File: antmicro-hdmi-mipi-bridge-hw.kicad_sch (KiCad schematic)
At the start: 0 parts

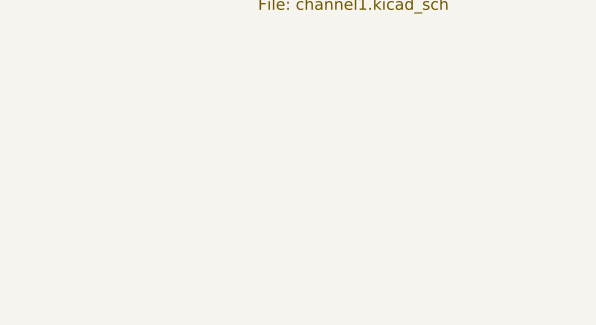
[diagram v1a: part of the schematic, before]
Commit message: [#58304] Fix DRC
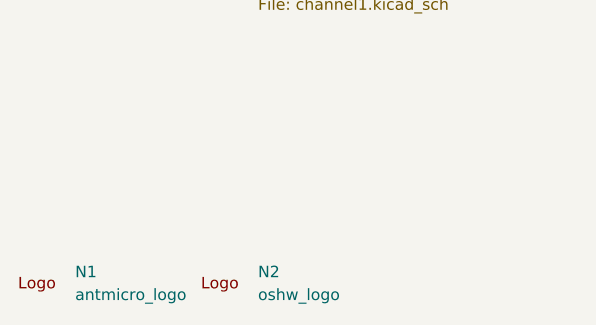
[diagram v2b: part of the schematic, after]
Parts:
- added N1: antmicro_logo, antmicro-footprints:antmicro-logo_scaled_20mm_mask, symbol antmicroMechanicalParts:antmicro_logo
- added N2: oshw_logo, antmicro-footprints:OSHW-Logo_7.5x8mm_Mask, symbol antmicroMechanicalParts:oshw_logo
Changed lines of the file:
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@@
+    )
+  )
+  (symbol (lib_id "antmicroMechanicalParts:antmicro_logo") (at 74.93 274.32 0) (unit 1)
+    (in_bom no) (on_board yes) (dnp no) (fields_autoplaced)
+    (property "Reference" "N1" (at 81.28 272.3362 0)
+      (effects (font (size 1.27 1.27) (thickness 0.15)) (justify left))
+    )
+    (property "Value" "antmicro_logo" (at 81.28 274.8762 0)
+      (effects (font (size 1.27 1.27) (thickness 0.15)) (justify left))
+    )
+    (property "Footprint" "antmicro-footprints:antmicro-logo_scaled_20mm_mask" (at 90.17 284.48 0)
+      (effects (font (size 1.27 1.27) (thickness 0.15)) (justify left bottom) hide)
+    )
+    (property "Datasheet" "" (at 90.17 287.02 0)
+      (effects (font (size 1.27 1.27) (thickness 0.15)) (justify left bottom) hide)
+    )
+    (property "MPN" "" (at 74.93 274.32 0)
+      (effects (font (size 1.27 1.27)) hide)
+    )
+    (property "Manufacturer" "" (at 90.17 294.64 0)
+      (effects (font (size 1.27 1.27) (thickness 0.15)) (justify left bottom) hide)
+    )
+    (property "Author" "Antmicro" (at 90.17 289.56 0)
+      (effects (font (size 1.27 1.27) (thickness 0.15)) (justify left bottom) hide)
+    )
+    (property "License" "Apache-2.0" (at 90.17 292.1 0)
+      (effects (font (size 1.27 1.27) (thickness 0.15)) (justify left bottom) hide)
+    )
+    (instances
+      (project "antmicro-hdmi-mipi-bridge-hw"
+        (path "/986e1fb1-d06b-4220-a40c-b0cc1c7adce3"
+          (reference "N1") (unit 1)
+        )
+      )
+    )
+  )
+  (symbol (lib_id "antmicroMechanicalParts:oshw_logo") (at 95.25 274.32 0) (unit 1)
+    (in_bom no) (on_board yes) (dnp no) (fields_autoplaced)
+    (property "Reference" "N2" (at 101.6 272.3362 0)
+      (effects (font (size 1.27 1.27) (thickness 0.15)) (justify left))
+    )
+    (property "Value" "oshw_logo" (at 101.6 274.8762 0)
+      (effects (font (size 1.27 1.27) (thickness 0.15)) (justify left))
+    )
+    (property "Footprint" "antmicro-footprints:OSHW-Logo_7.5x8mm_Mask" (at 110.49 284.48 0)
+      (effects (font (size 1.27 1.27) (thickness 0.15)) (justify left bottom) hide)
+    )
+    (property "Datasheet" "" (at 110.49 287.02 0)
+      (effects (font (size 1.27 1.27) (thickness 0.15)) (justify left bottom) hide)
+    )
+    (property "Author" "Antmicro" (at 110.49 289.56 0)
+      (effects (font (size 1.27 1.27) (thickness 0.15)) (justify left bottom) hide)
+    )
+    (property "License" "Apache-2.0" (at 110.49 292.1 0)
+      (effects (font (size 1.27 1.27) (thickness 0.15)) (justify left bottom) hide)
+    )
+    (property "MPN" "" (at 95.25 274.32 0)
+      (effects (font (size 1.27 1.27)) hide)
+    )
+    (property "Manufacturer" "" (at 110.49 294.64 0)
+      (effects (font (size 1.27 1.27) (thickness 0.15)) (justify left bottom) hide)
+    )
+    (instances
+      (project "antmicro-hdmi-mipi-bridge-hw"
+        (path "/986e1fb1-d06b-4220-a40c-b0cc1c7adce3"
+          (reference "N2") (unit 1)
+        )
+      )
     )
   )
